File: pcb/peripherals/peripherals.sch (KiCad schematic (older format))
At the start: 16 parts, among them J1 JST XH, J2 JST XH, J3 Conn_01x03, J9 JST XH, U1 DFPlayer_Mini

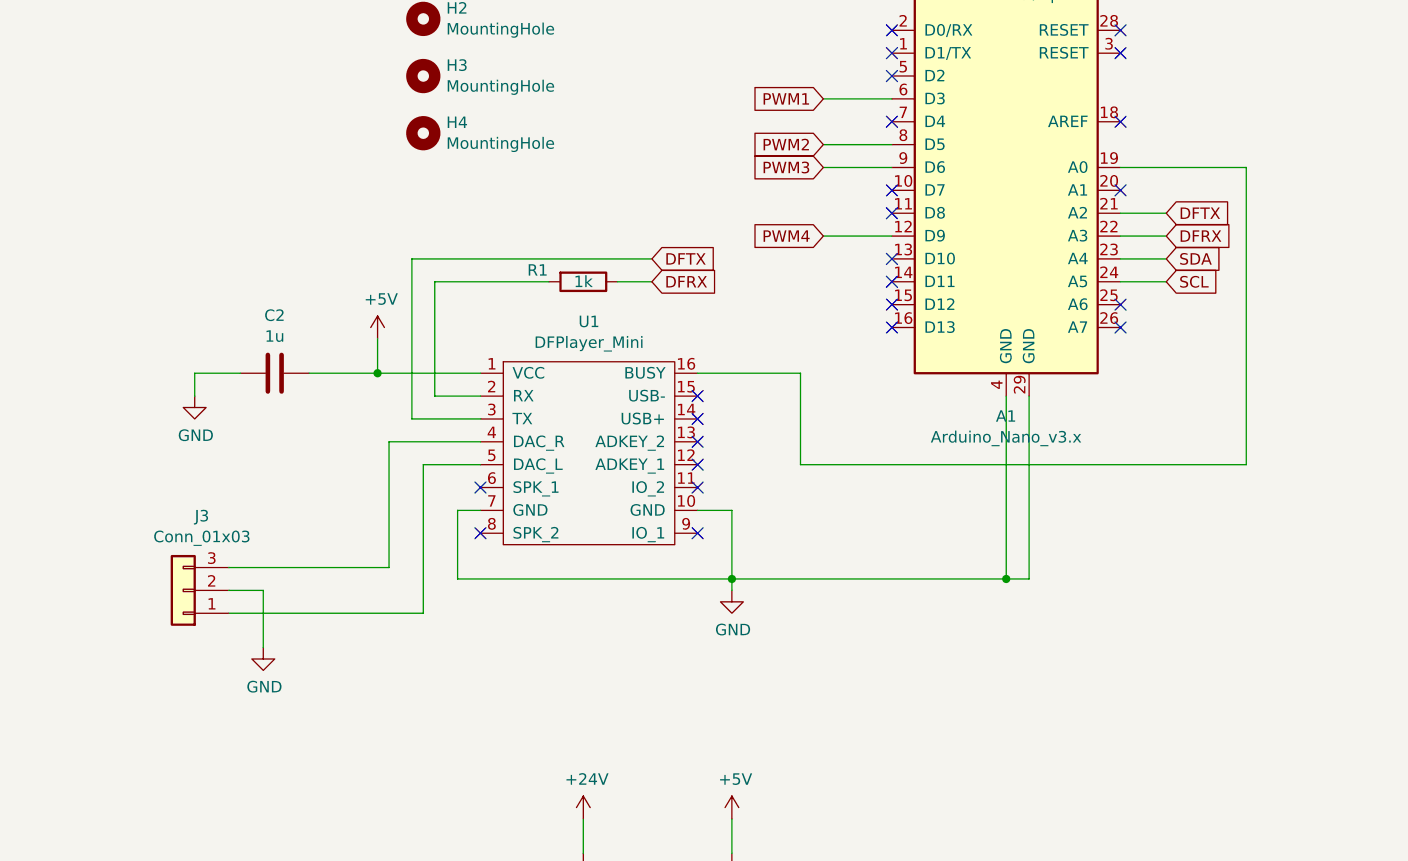
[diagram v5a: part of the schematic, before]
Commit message: Remove DFPlayer.
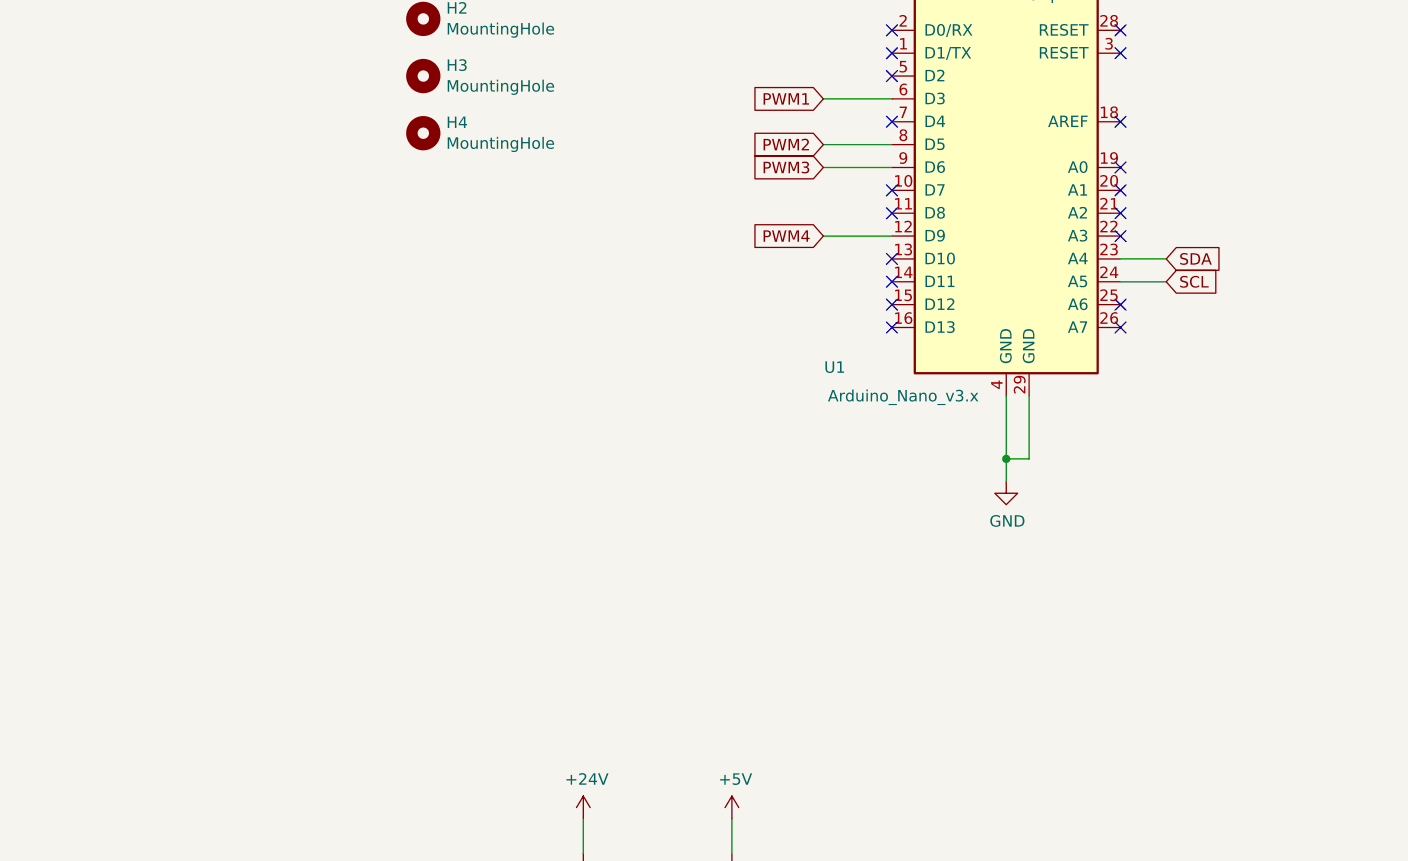
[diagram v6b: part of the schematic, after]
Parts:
- removed C2: 1u, Capacitor_SMD:C_0603_1608Metric, symbol Device:C
- removed J3: Conn_01x03, Connector_JST:JST_XH_B03B-XH-A_1x03_P2.50mm_Vertical, symbol Connector_Generic:Conn_01x03
- removed R1: 1k, Resistor_SMD:R_0603_1608Metric, symbol Device:R
- removed U1: DFPlayer_Mini, Peripherals:DFPlayer, symbol peripherals-rescue:DFPlayer_Mini-dfplayer
- renumbered A1 to U1
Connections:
- net DFRX: no longer names the net of U1.22 (A3)
- net DFTX: no longer names the net of U1.21 (A2)
- no-connect marks 26 -> 21
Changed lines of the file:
@@
 EESchema Schematic File Version 4
-LIBS:peripherals-cache
-EELAYER 29 0
+EELAYER 30 0
 EELAYER END
 $Descr A4 11693 8268
@@
 $EndDescr
 $Comp
-L MCU_Module:Arduino_Nano_v3.x A1
+L MCU_Module:Arduino_Nano_v3.x U1
 U 1 1 5D190561
 P 5450 3550
-F 0 "A1" H 5450 2461 50  0000 C CNN
-F 1 "Arduino_Nano_v3.x" H 5450 2370 50  0000 C CNN
+F 0 "U1" H 4700 2675 50  0000 C CNN
+F 1 "Arduino_Nano_v3.x" H 5000 2550 50  0000 C CNN
 F 2 "Module:Arduino_Nano" H 5600 2600 50  0001 L CNN
 F 3 "http://www.mouser.com/pdfdocs/Gravitech_Arduino_Nano3_0.pdf" H 5450 2550 50  0001 C CNN
@@
 	1    0    0    -1
 $EndComp
-$Comp
-L peripherals-rescue:DFPlayer_Mini-dfplayer U1
-U 1 1 5D1A34FC
-P 3650 4750
-F 0 "U1" H 3625 5275 50  0000 C CNN
-F 1 "DFPlayer_Mini" H 3625 5184 50  0000 C CNN
-F 2 "Peripherals:DFPlayer" H 3550 4700 50  0001 C CNN
-F 3 "" H 3550 4700 50  0000 C CNN
-	1    3650 4750
-	1    0    0    -1
-$EndComp
-$Comp
-L power:+5V #PWR0103
-U 1 1 5D1A4428
-P 2700 4300
-F 0 "#PWR0103" H 2700 4150 50  0001 C CNN
-F 1 "+5V" H 2715 4473 50  0000 C CNN
-F 2 "" H 2700 4300 50  0001 C CNN
-F 3 "" H 2700 4300 50  0001 C CNN
-	1    2700 4300
-	1    0    0    -1
-$EndComp
-Wire Wire Line
-	2700 4300 2700 4450
-Wire Wire Line
-	2700 4450 3150 4450
-$Comp
-L power:GND #PWR0104
-U 1 1 5D1A49F6
-P 4250 5400
-F 0 "#PWR0104" H 4250 5150 50  0001 C CNN
-F 1 "GND" H 4255 5227 50  0000 C CNN
-F 2 "" H 4250 5400 50  0001 C CNN
-F 3 "" H 4250 5400 50  0001 C CNN
-	1    4250 5400
-	1    0    0    -1
-$EndComp
-Wire Wire Line
-	4100 5050 4250 5050
-Wire Wire Line
-	4250 5050 4250 5350
-Wire Wire Line
-	3150 5050 3050 5050
-Wire Wire Line
-	3050 5050 3050 5350
-Wire Wire Line
-	3050 5350 4250 5350
-Connection ~ 4250 5350
-Wire Wire Line
-	4250 5350 4250 5400
-Wire Wire Line
-	4250 5350 5450 5350
-Wire Wire Line
-	5550 5350 5550 4550
-Wire Wire Line
-	5450 4550 5450 5350
-Connection ~ 5450 5350
-Wire Wire Line
-	5450 5350 5550 5350
 Wire Wire Line
 	1400 1250 1950 1250
@@
 	8550 1650 8700 1650
 Connection ~ 8700 1650
-Wire Wire Line
-	2850 3950 2850 4650
-Wire Wire Line
-	2850 4650 3150 4650
-$Comp
-L Device:R R1
-U 1 1 5D1C81CA
-P 3600 4050
-F 0 "R1" V 3550 3850 50  0000 C CNN
-F 1 "1k" V 3600 4050 50  0000 C CNN
-F 2 "Resistor_SMD:R_0603_1608Metric" V 3530 4050 50  0001 C CNN
-F 3 "~" H 3600 4050 50  0001 C CNN
-	1    3600 4050
-	0    1    1    0
-$EndComp
-Wire Wire Line
-	3450 4050 2950 4050
-Wire Wire Line
-	2950 4050 2950 4550
-Wire Wire Line
-	2950 4550 3150 4550
 $Comp
 L Device:CP C1
@@
 Wire Wire Line
 	3600 6850 3600 6900
-$Comp
-L power:GND #PWR0113
-U 1 1 5D1ACF80
-P 2200 5650
-F 0 "#PWR0113" H 2200 5400 50  0001 C CNN
-F 1 "GND" H 2205 5477 50  0000 C CNN
-F 2 "" H 2200 5650 50  0001 C CNN
-F 3 "" H 2200 5650 50  0001 C CNN
-	1    2200 5650
-	1    0    0    -1
-$EndComp
 $Comp
 L power:+5V #PWR0115
@@
 NoConn ~ 4950 3950
 NoConn ~ 5950 4150
-Wire Wire Line
-	5950 3550 6500 3550
-Wire Wire Line
-	6500 3550 6500 4850
-Wire Wire Line
-	6500 4850 4550 4850
-Wire Wire Line
-	4550 4850 4550 4450
-Wire Wire Line
-	4550 4450 4100 4450
 NoConn ~ 5950 4250
-NoConn ~ 4100 4550
-NoConn ~ 4100 4650
-NoConn ~ 4100 4750
-NoConn ~ 4100 4850
-NoConn ~ 4100 4950
-NoConn ~ 4100 5150
-Wire Wire Line
-	2900 4850 3150 4850
-Wire Wire Line
-	3150 4750 2750 4750
-NoConn ~ 3150 4950
-NoConn ~ 3150 5150
 $Comp
 L power:PWR_FLAG #FLG0101
@@
 Wire Wire Line
 	6500 1200 6650 1200
-$Comp
-L Device:C C2
-U 1 1 5D1D601E
-P 2250 4450
-F 0 "C2" V 1998 4450 50  0000 C CNN
-F 1 "1u" V 2089 4450 50  0000 C CNN
-F 2 "Capacitor_SMD:C_0603_1608Metric" H 2288 4300 50  0001 C CNN
-F 3 "~" H 2250 4450 50  0001 C CNN
-	1    2250 4450
-	0    1    1    0
-$EndComp
-$Comp
-L power:GND #PWR01
-U 1 1 5D1D6BB2
-P 1900 4550
-F 0 "#PWR01" H 1900 4300 50  0001 C CNN
-F 1 "GND" H 1905 4377 50  0000 C CNN
-F 2 "" H 1900 4550 50  0001 C CNN
-F 3 "" H 1900 4550 50  0001 C CNN
-	1    1900 4550
-	1    0    0    -1
-$EndComp
-Wire Wire Line
-	1900 4550 1900 4450
-Wire Wire Line
-	1900 4450 2100 4450
-Wire Wire Line
-	2400 4450 2700 4450
-Connection ~ 2700 4450
 $Comp
 L Mechanical:MountingHole H1
@@
 	5650 2450 5650 2550
 $Comp
-L Connector_Generic:Conn_01x03 J3
-U 1 1 5DAC0F2C
-P 1850 5400
-F 0 "J3" H 1768 5075 50  0000 C CNN
-F 1 "Conn_01x03" H 1768 5166 50  0000 C CNN
-F 2 "Connector_JST:JST_XH_B03B-XH-A_1x03_P2.50mm_Vertical" H 1850 5400 50  0001 C CNN
-F 3 "~" H 1850 5400 50  0001 C CNN
-	1    1850 5400
-	-1   0    0    1
-$EndComp
-Wire Wire Line
-	2750 5300 2050 5300
-Wire Wire Line
-	2750 4750 2750 5300
-Wire Wire Line
-	2900 4850 2900 5500
-Wire Wire Line
-	2900 5500 2050 5500
-Wire Wire Line
-	2050 5400 2200 5400
-Wire Wire Line
-	2200 5400 2200 5650
-$Comp
 L power:GNDPWR #PWR0108
 U 1 1 5DADDBBA
@@
 	1    0    0    -1
 $EndComp
-Text GLabel 3900 4050 2    50   Input ~ 0
-DFRX
-Wire Wire Line
-	3900 4050 3750 4050
-Text GLabel 6150 3850 2    50   Input ~ 0
-DFRX
-Wire Wire Line
-	5950 3850 6150 3850
 NoConn ~ 4950 4050
-Text GLabel 3900 3950 2    50   Input ~ 0
-DFTX
-Wire Wire Line
-	3900 3950 2850 3950
-Text GLabel 6150 3750 2    50   Input ~ 0
-DFTX
-Wire Wire Line
-	6150 3750 5950 3750
 NoConn ~ 4950 4250
 NoConn ~ 4950 4150
@@
 	4600 6850 4600 6950
 Connection ~ 4250 6850
+$Comp
+L power:GND #PWR0103
+U 1 1 5F790F99
+P 5450 4925
+F 0 "#PWR0103" H 5450 4675 50  0001 C CNN
+F 1 "GND" H 5455 4752 50  0000 C CNN
+F 2 "" H 5450 4925 50  0001 C CNN
+F 3 "" H 5450 4925 50  0001 C CNN
+	1    5450 4925
+	1    0    0    -1
+$EndComp
+Wire Wire Line
+	5450 4925 5450 4825
+Wire Wire Line
+	5550 4550 5550 4825
+Wire Wire Line
+	5550 4825 5450 4825
+Connection ~ 5450 4825
+Wire Wire Line
+	5450 4825 5450 4550
+NoConn ~ 5950 3550
+NoConn ~ 5950 3750
+NoConn ~ 5950 3850
 $EndSCHEMATC

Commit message: Work on layout.
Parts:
- removed R6: 100R, Resistor_SMD:R_0603_1608Metric, symbol Device:R
- added J10: Conn_01x04, Connector_JST:JST_XH_B04B-XH-A_1x04_P2.50mm_Vertical, symbol Connector_Generic:Conn_01x04
- added J4, J9: Conn_01x08, Connector_JST:JST_XH_B08B-XH-A_1x08_P2.50mm_Vertical, symbol Connector_Generic:Conn_01x08
- renumbered C3 to C2, J9 to J3
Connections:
- net GNDPWR is gone; now on net GND: C1.2, J3.2 (Pin_2)
- net +5V: now also J10.2 (Pin_2), J4.8 (Pin_8), J9.8 (Pin_8)
- net GND: now also J10.1 (Pin_1), J4.1 (Pin_1), J9.1 (Pin_1)
- net D7: now reaches U1.10 (D7)
- net D7: now also J4.2 (Pin_2)
- net D8: now reaches U1.11 (D8)
- net D8: now also J4.3 (Pin_3)
- net D10: now reaches U1.13 (D10)
- net D10: now also J4.4 (Pin_4)
- net D11: now reaches U1.14 (D11)
- net D11: now also J4.5 (Pin_5)
- net D12: now reaches U1.15 (D12)
- net D12: now also J4.6 (Pin_6)
- net D13: now reaches U1.16 (D13)
- net D13: now also J4.7 (Pin_7)
- net A0: now reaches U1.19 (A0)
- net A0: now also J9.2 (Pin_2)
- net A1: now reaches U1.20 (A1)
- net A1: now also J9.3 (Pin_3)
- net A2: now reaches U1.21 (A2)
- net A2: now also J9.4 (Pin_4)
- net A3: now reaches U1.22 (A3)
- net A3: now also J9.5 (Pin_5)
- net A6: now reaches U1.25 (A6)
- net A6: now also J9.6 (Pin_6)
- net A7: now reaches U1.26 (A7)
- net A7: now also J9.7 (Pin_7)
- net MPRX: now reaches U1.5 (D2)
- net MPRX: now also J10.4 (Pin_4)
- net MPTX: now reaches U1.7 (D4)
- net MPTX: now also J10.3 (Pin_3)
- no-connect marks 21 -> 7
